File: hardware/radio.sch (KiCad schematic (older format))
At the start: 19 parts, among them U3 AT86RF231, Y1 NX3225SA-16MHz-15ppm

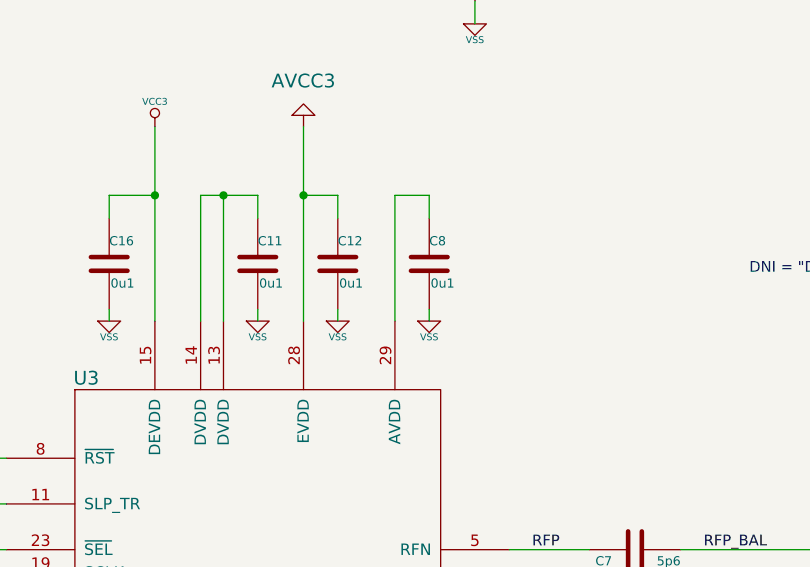
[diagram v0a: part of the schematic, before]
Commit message: Corrections to C8/12 decoupling caps. Should be 0u01, not 0u1 (not critical).
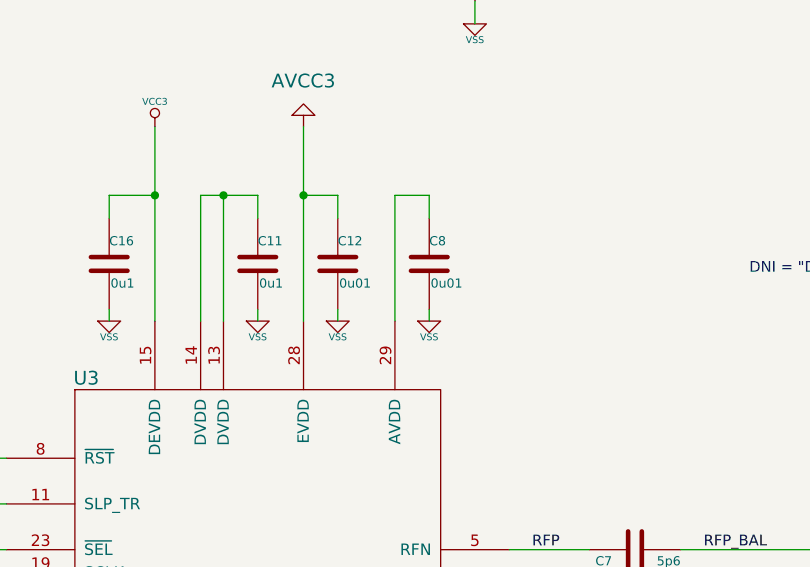
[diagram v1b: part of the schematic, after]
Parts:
- C12, C8: value 0u1 -> 0u01
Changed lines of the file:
@@
 $Descr A4 11693 8268
 encoding utf-8
-Sheet 3 6
+Sheet 2 6
 Title "FREAKDUINO-CHIBI 2.4GHz"
-Date "18 jul 2013"
+Date "3 mar 2014"
 Rev "v2.1a"
 Comp "KiCAD version by Gruvin"
@@
 P 4850 2750
 F 0 "C12" H 4850 2850 40  0000 L CNN
-F 1 "0u1" H 4856 2665 40  0000 L CNN
+F 1 "0u01" H 4856 2665 40  0000 L CNN
 F 2 "" H 4888 2600 30  0000 C CNN
 F 3 "" H 4850 2750 60  0000 C CNN
@@
 P 5250 2750
 F 0 "C8" H 5250 2850 40  0000 L CNN
-F 1 "0u1" H 5256 2665 40  0000 L CNN
+F 1 "0u01" H 5256 2665 40  0000 L CNN
 F 2 "" H 5288 2600 30  0000 C CNN
 F 3 "" H 5250 2750 60  0000 C CNN
